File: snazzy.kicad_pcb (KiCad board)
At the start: 2 copper layers, 66 x 59.7 mm, 30 parts, among them J1 Conn_01x03, J2 Conn_01x03, SW1 BTN_START, SW10 BTN_DOWN, SW11 BTN_L, SW12 BTN_R, SW2 BTN_SELECT, SW3 BTN_A, SW4 BTN_B, SW5 BTN_X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

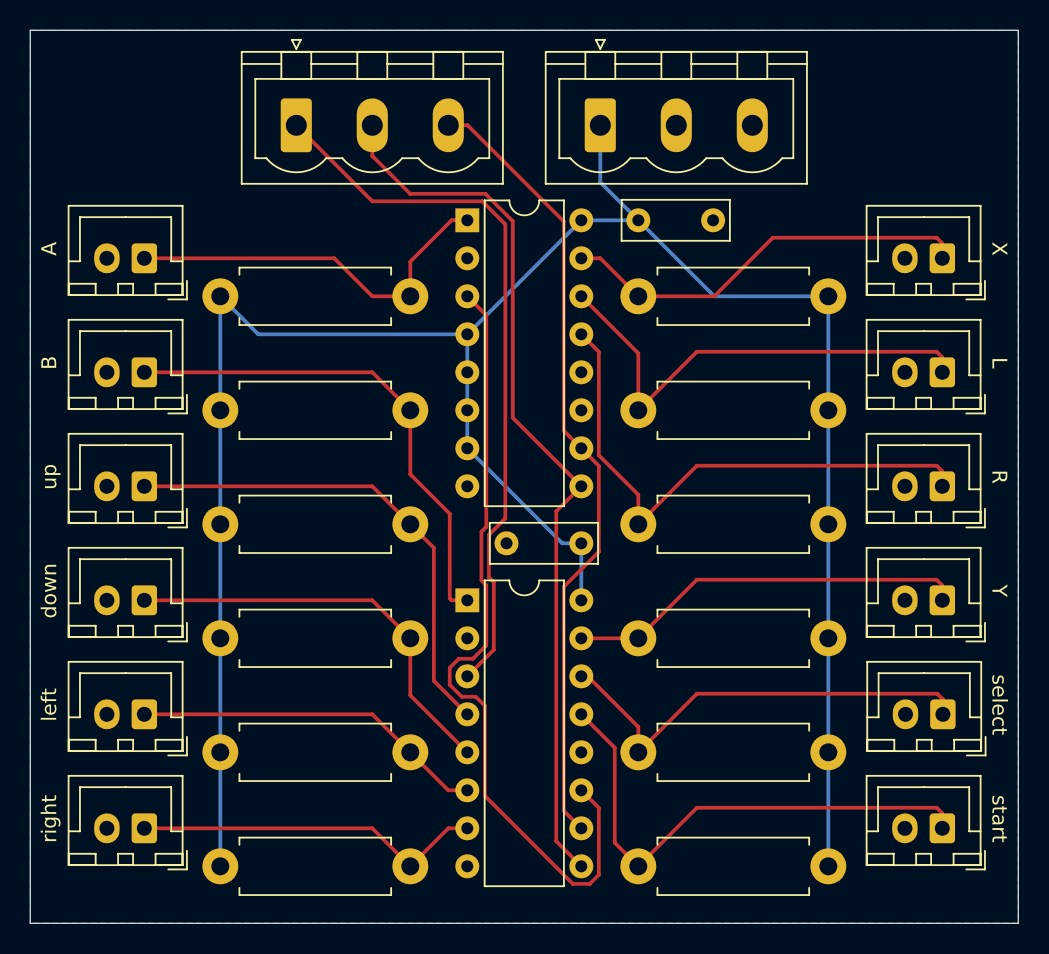
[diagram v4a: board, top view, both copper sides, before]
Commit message: PCB: Support left^right and down^up
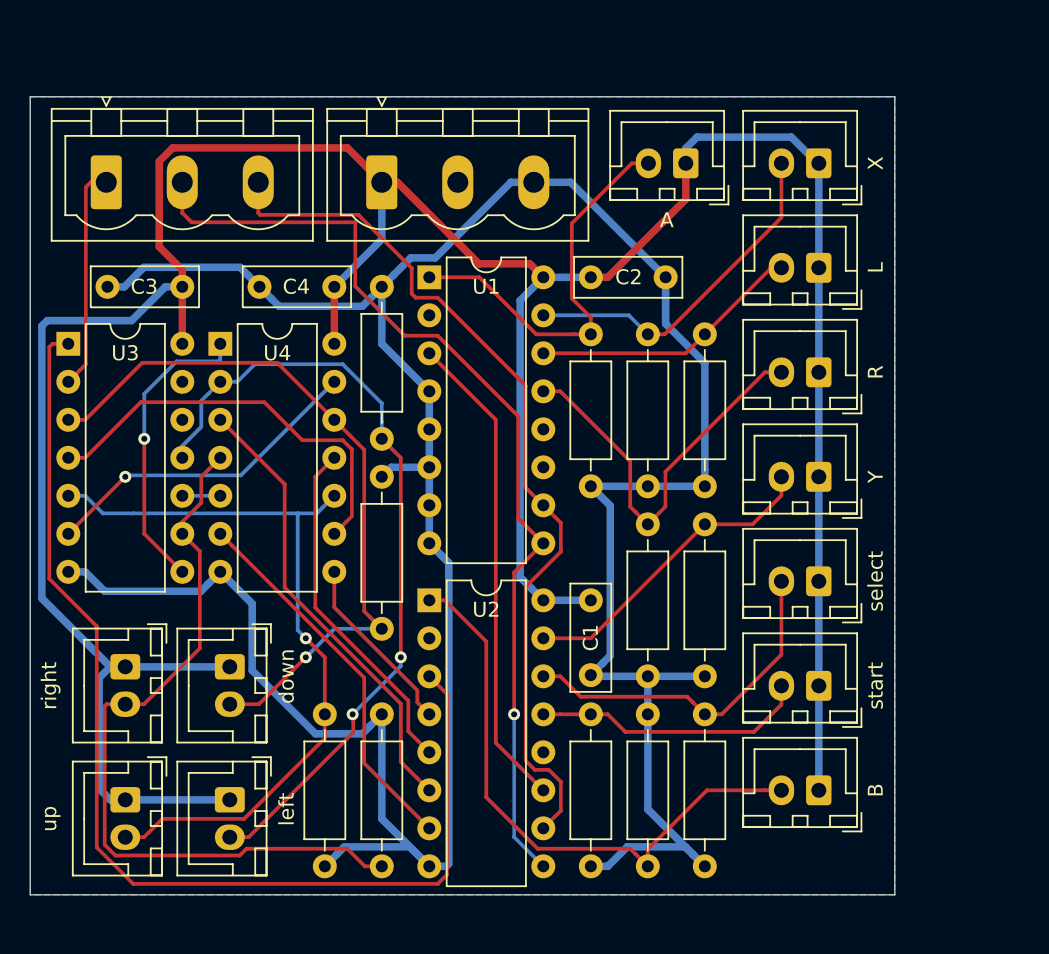
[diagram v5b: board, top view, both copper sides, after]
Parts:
- added C3: 100n, Capacitor_THT:C_Rect_L7.0mm_W2.5mm_P5.00mm, F.Cu at (118.1, 87.0)
- added C4: 100n, Capacitor_THT:C_Rect_L7.0mm_W2.5mm_P5.00mm, F.Cu at (128.3, 87.0)
- added U3: 74HC04, Package_DIP:DIP-14_W7.62mm, F.Cu at (110.5, 90.8)
- added U4: 74HC08, Package_DIP:DIP-14_W7.62mm, F.Cu at (120.7, 90.8)
- R1, R10, R11, R12, R2, R3, R4, R5, R6, R7, R8, R9: footprint Resistor_THT:R_Axial_DIN0411_L9.9mm_D3.6mm_P12.70mm_Horizontal -> Resistor_THT:R_Axial_DIN0207_L6.3mm_D2.5mm_P10.16mm_Horizontal
- moved SW4 53.0 mm to (160.7, 120.7)
- moved R4 41.8 mm to (149.2, 125.7), turned to 90 degrees
- moved SW3 36.7 mm to (151.8, 78.7)
- moved R3 24.9 mm to (145.4, 90.2), turned to 270 degrees
- moved R7 23.6 mm to (131.4, 97.2), turned to 90 degrees
- moved SW9 21.0 mm to (114.3, 121.3), turned to 270 degrees
- moved R1 18.8 mm to (145.4, 115.6), turned to 270 degrees
- moved J1 15.1 mm to (131.4, 80.0)
- moved R9 14.5 mm to (127.6, 115.6), turned to 270 degrees
- moved J2 13.3 mm to (113.0, 80.0)
- moved SW1 12.6 mm to (160.7, 113.7)
- moved R5 12.3 mm to (149.2, 90.2), turned to 270 degrees
- moved SW2 12.2 mm to (160.7, 106.7)
- moved R12 12.1 mm to (149.2, 102.9), turned to 270 degrees
- moved SW6 11.7 mm to (160.7, 99.7)
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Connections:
- R1 pad 1: +5V -> /BTN_START
- R1 pad 2: /BTN_START -> GND
- R10 pad 1: +5V -> /BTN_DOWN
- R10 pad 2: /BTN_DOWN -> GND
- R11 pad 1: +5V -> /BTN_L
- R11 pad 2: /BTN_L -> GND
- R12 pad 1: +5V -> /BTN_R
- R12 pad 2: /BTN_R -> GND
- R2 pad 1: +5V -> /BTN_SELECT
- R2 pad 2: /BTN_SELECT -> GND
- R3 pad 1: +5V -> /BTN_A
- R3 pad 2: /BTN_A -> GND
- R4 pad 1: +5V -> /BTN_B
- R4 pad 2: /BTN_B -> GND
- R5 pad 1: +5V -> /BTN_X
- R5 pad 2: /BTN_X -> GND
- R6 pad 1: +5V -> /BTN_Y
- R6 pad 2: /BTN_Y -> GND
- R7 pad 1: +5V -> /BTN_LEFT
- R7 pad 2: /BTN_LEFT -> GND
- R8 pad 1: +5V -> /BTN_RIGHT
- R8 pad 2: /BTN_RIGHT -> GND
- R9 pad 1: +5V -> /BTN_UP
- R9 pad 2: /BTN_UP -> GND
- SW1 pad 1: /BTN_START -> +5V
- SW1 pad 2: GND -> /BTN_START
- SW10 pad 1: /BTN_DOWN -> +5V
- SW10 pad 2: GND -> /BTN_DOWN
- SW11 pad 1: /BTN_L -> +5V
- SW11 pad 2: GND -> /BTN_L
- SW12 pad 1: /BTN_R -> +5V
- SW12 pad 2: GND -> /BTN_R
- SW2 pad 1: /BTN_SELECT -> +5V
- SW2 pad 2: GND -> /BTN_SELECT
- SW3 pad 1: /BTN_A -> +5V
- SW3 pad 2: GND -> /BTN_A
- SW4 pad 1: /BTN_B -> +5V
- SW4 pad 2: GND -> /BTN_B
- SW5 pad 1: /BTN_X -> +5V
- SW5 pad 2: GND -> /BTN_X
- SW6 pad 1: /BTN_Y -> +5V
- SW6 pad 2: GND -> /BTN_Y
- SW7 pad 1: /BTN_LEFT -> +5V
- SW7 pad 2: GND -> /BTN_LEFT
- SW8 pad 1: /BTN_RIGHT -> +5V
- SW8 pad 2: GND -> /BTN_RIGHT
- SW9 pad 1: /BTN_UP -> +5V
- SW9 pad 2: GND -> /BTN_UP
- U1 pad 4: +5V -> GND
- U1 pad 5: +5V -> GND
- U1 pad 6: +5V -> GND
- U1 pad 7: +5V -> GND
- U2 pad 3: SNES_data1 -> Net-(U2-Pad3)
- U2 pad 4: /BTN_UP -> /VBTN_UP
- U2 pad 5: /BTN_DOWN -> /VBTN_DOWN
- U2 pad 6: /BTN_LEFT -> /VBTN_LEFT
- U2 pad 7: /BTN_RIGHT -> /VBTN_RIGHT
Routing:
- net GND: track 0.00 -> 206.4 mm
- net Net-(U2-Pad3): track 0.00 -> 74.5 mm
- net +5V: track 152.2 -> 208.2 mm
- net SNES_data1: track 48.2 -> 15.0 mm
- net /VBTN_LEFT: track 0.00 -> 30.6 mm
- net /BTN_LEFT: track 23.7 -> 53.5 mm, vias 0 -> 2
- net Net-(U3-Pad4): track 0.00 -> 27.9 mm
- net /BTN_RIGHT: track 23.7 -> 51.0 mm
- net /VBTN_RIGHT: track 0.00 -> 25.5 mm
- net /VBTN_DOWN: track 0.00 -> 23.4 mm
- net Net-(U3-Pad6): track 0.00 -> 22.0 mm, vias 0 -> 1
- net Net-(U1-Pad3): track 53.7 -> 32.4 mm
- net /BTN_DOWN: track 28.0 -> 48.5 mm, vias 0 -> 1
- net Net-(U3-Pad8): track 0.00 -> 20.0 mm, vias 0 -> 1
- net /BTN_UP: track 33.1 -> 51.2 mm, vias 0 -> 1
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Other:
- board size 66 x 59.7 mm -> 57.8 x 53.3 mm
- net class power added: clearance 0.25, trace_width 0.5, via_dia 0.8, via_drill 0.4
- board text removed: "A"
- board text removed: "B"
- board text removed: "L"
- board text removed: "R"
- board text removed: "X"
- board text removed: "Y"
- board text removed: "down"
- board text removed: "left"
- board text removed: "right"
- board text removed: "select"
- board text removed: "start"
- board text removed: "up"
